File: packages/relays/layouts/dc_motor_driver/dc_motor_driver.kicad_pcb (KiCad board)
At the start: 2 copper layers, 4 parts

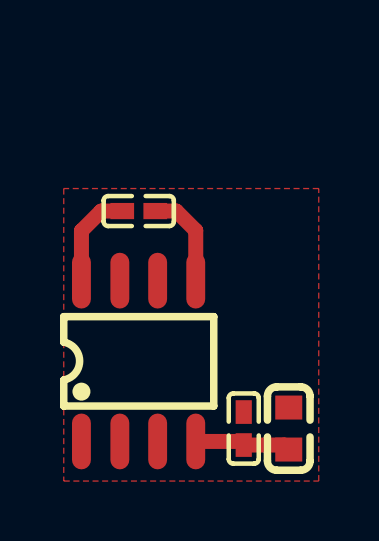
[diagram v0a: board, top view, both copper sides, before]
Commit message: Manually fix fp lib tables
fix some small bugs
fix package only modules (e.g. logos)
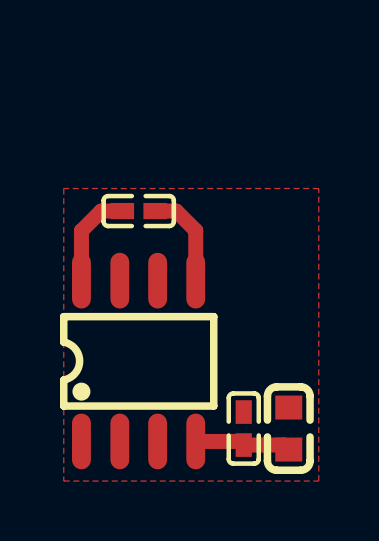
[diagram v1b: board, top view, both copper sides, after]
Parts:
- C1: footprint atopile:C0402-b3ef17 -> Samsung_Electro_Mechanics_CL05B104KO5NNNC:C0402
- C2: footprint atopile:C0603-bd72f6 -> Samsung_Electro_Mechanics_CL10A475KO8NNNC:C0603
- C3: footprint atopile:C0402-b3ef17 -> FH_0402CG101J500NT:C0402
- U1: footprint atopile:SOP-8_L4.9-W3.9-P1.27-LS6.0-BL-0d1ac6 -> Shenzhen_Fuman_Elec_TC118S:SOP-8_L4.9-W3.9-P1.27-LS6.0-BL

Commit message: Update 3D model locations
fix missing renders
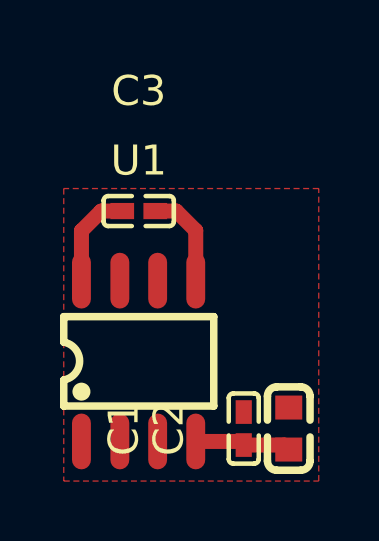
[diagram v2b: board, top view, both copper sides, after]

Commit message: rebuild all packages & regenerate images of changed layouts (silk)
Add new scripts for version bump and build (based on atopile/packages)
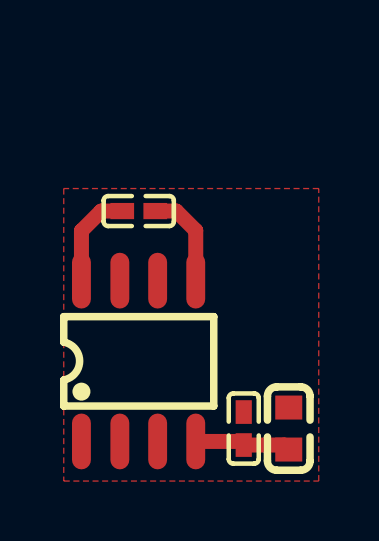
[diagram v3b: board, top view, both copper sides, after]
